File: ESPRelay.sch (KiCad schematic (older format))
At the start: 23 parts, among them J1 RELAY1, J2 RELAY2, J3 SENSOR_1, J4 SENSOR_2, K1 G5Q-1, K2 G5Q-1, Q1 2N3904, Q2 2N3904, U1 NodeMCU_1.0_(ESP-12E), U2 EL817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

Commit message: Fixed misconnected sensor inputs
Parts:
- U1: symbol ESP8266:NodeMCU_1.0_(ESP-12E) -> ESPRelay-rescue:NodeMCU_1.0_(ESP-12E)-ESP8266
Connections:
- net at U1.22 (D6(GPIO12)): now also J4.2 (Pin_2)
- net at U1.23 (D5(GPIO14)): now also J3.2 (Pin_2)
- net at U1.26 (D4(GPIO2)): no longer J4.2 (Pin_2)
- net at U1.27 (D3(GPIO0)): no longer J3.2 (Pin_2)
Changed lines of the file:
@@
 NoConn ~ 2700 3200
 NoConn ~ 2700 3500
-NoConn ~ 2700 3700
-NoConn ~ 2700 3800
 NoConn ~ 2700 3900
 NoConn ~ 2700 4000
@@
 NoConn ~ 1100 4200
 $Comp
-L ESP8266:NodeMCU_1.0_(ESP-12E) U1
+L ESPRelay-rescue:NodeMCU_1.0_(ESP-12E)-ESP8266 U1
 U 1 1 60060E77
 P 1900 3700
@@
 $EndComp
 Wire Wire Line
-	2700 3300 3500 3300
-Wire Wire Line
-	3500 3300 3500 3200
-Wire Wire Line
-	3500 3200 3850 3200
-Wire Wire Line
-	2700 3400 3500 3400
-Wire Wire Line
-	3500 3400 3500 3500
-Wire Wire Line
-	3500 3500 3850 3500
-Wire Wire Line
 	3750 2250 3750 3100
 Wire Wire Line
@@
 Wire Wire Line
 	3750 3100 3750 3300
+Wire Wire Line
+	2700 3700 3300 3700
+Wire Wire Line
+	3300 3700 3300 3200
+Wire Wire Line
+	3300 3200 3850 3200
+Wire Wire Line
+	2700 3800 3400 3800
+Wire Wire Line
+	3400 3800 3400 3500
+Wire Wire Line
+	3400 3500 3850 3500
+NoConn ~ 2700 3300
+NoConn ~ 2700 3400
 $EndSCHEMATC

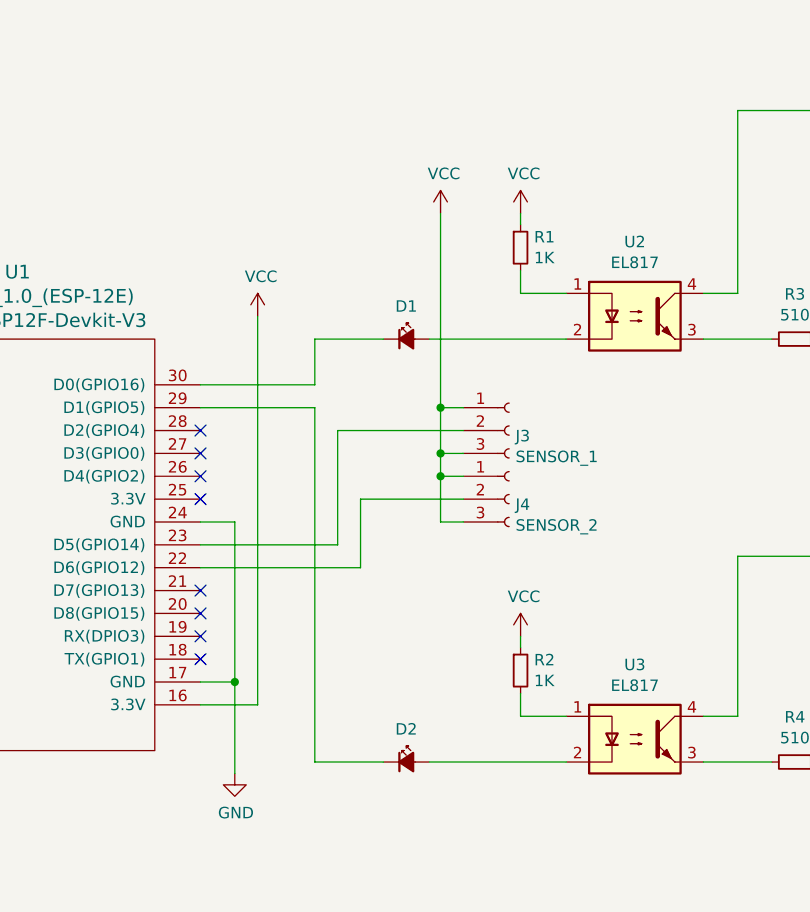
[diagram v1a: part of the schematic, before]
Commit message: Fix error with relay connections to NodeMCU. Include README.md and git ignore file.
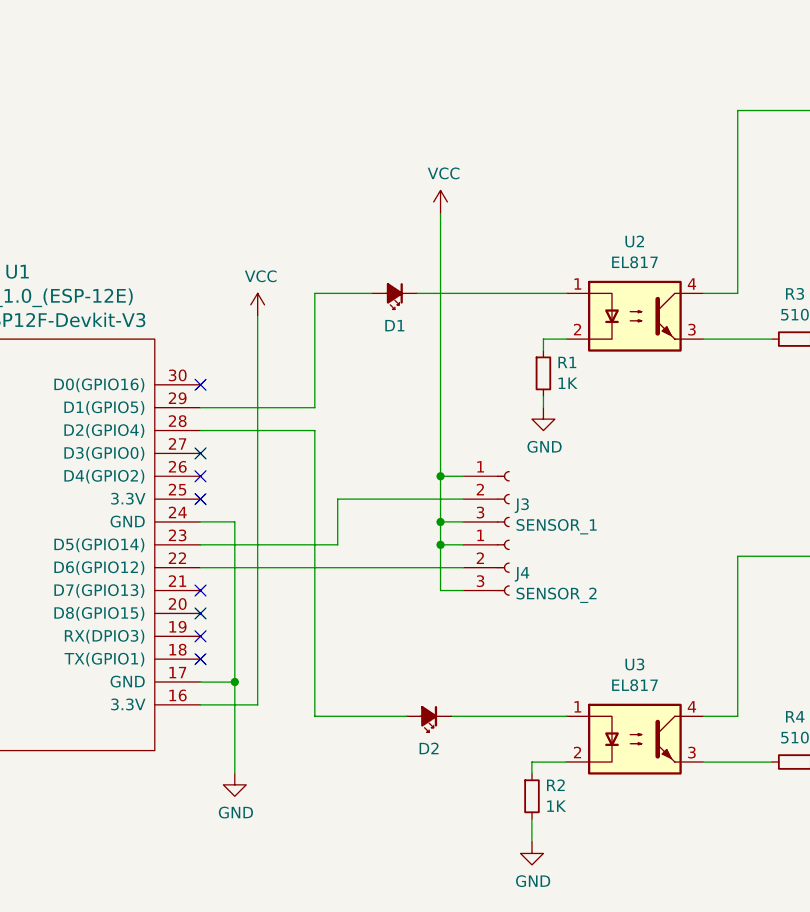
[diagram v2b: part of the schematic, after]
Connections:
- net GND: now also R1.2, R2.2
- net VCC: no longer R1.1, R2.1
- net at U2.1: now also D1.1 (K); no longer R1.2
- net at U2.2: now also R1.1; no longer D1.2 (A)
- net at U3.1: now also D2.1 (K); no longer R2.2
- net at U3.2: now also R2.1; no longer D2.2 (A)
- net at U1.30 (D0(GPIO16)): no longer D1.1 (K)
- net at U1.29 (D1(GPIO5)): now also D1.2 (A); no longer D2.1 (K)
- net at U1.28 (D2(GPIO4)): now also D2.2 (A)
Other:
- moved on the sheet: D1, D2, J3, J4, R1, R2
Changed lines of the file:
@@
 L Device:LED_Small_ALT D1
 U 1 1 60045D7A
-P 3600 2800
-F 0 "D1" H 3600 2943 50  0000 C CNN
-F 1 "LED_Small_ALT" H 3600 2944 50  0001 C CNN
-F 2 "LED_THT:LED_D5.0mm" V 3600 2800 50  0001 C CNN
-F 3 "~" V 3600 2800 50  0001 C CNN
-	1    3600 2800
-	1    0    0    -1
+P 3550 2600
+F 0 "D1" H 3550 2743 50  0000 C CNN
+F 1 "LED_Small_ALT" H 3550 2744 50  0001 C CNN
+F 2 "LED_THT:LED_D5.0mm" V 3550 2600 50  0001 C CNN
+F 3 "~" V 3550 2600 50  0001 C CNN
+	1    3550 2600
+	-1   0    0    1
 $EndComp
 $Comp
 L Device:LED_Small_ALT D2
 U 1 1 600472E3
-P 3600 4650
-F 0 "D2" H 3600 4793 50  0000 C CNN
-F 1 "LED_Small_ALT" H 3600 4794 50  0001 C CNN
-F 2 "LED_THT:LED_D5.0mm" V 3600 4650 50  0001 C CNN
-F 3 "~" V 3600 4650 50  0001 C CNN
-	1    3600 4650
-	1    0    0    -1
-$EndComp
-Wire Wire Line
-	2700 3000 3200 3000
-Wire Wire Line
-	3200 3000 3200 2800
-Wire Wire Line
-	3200 2800 3500 2800
-Wire Wire Line
-	2700 3100 3200 3100
-$Comp
-L power:VCC #PWR05
-U 1 1 6004C243
-P 4100 2250
-F 0 "#PWR05" H 4100 2100 50  0001 C CNN
-F 1 "VCC" H 4115 2423 50  0000 C CNN
-F 2 "" H 4100 2250 50  0001 C CNN
-F 3 "" H 4100 2250 50  0001 C CNN
-	1    4100 2250
-	1    0    0    -1
+P 3700 4450
+F 0 "D2" H 3700 4593 50  0000 C CNN
+F 1 "LED_Small_ALT" H 3700 4594 50  0001 C CNN
+F 2 "LED_THT:LED_D5.0mm" V 3700 4450 50  0001 C CNN
+F 3 "~" V 3700 4450 50  0001 C CNN
+	1    3700 4450
+	-1   0    0    1
 $EndComp
 $Comp
 L Device:R_Small R1
 U 1 1 6004D44F
-P 4100 2400
-F 0 "R1" H 4159 2446 50  0000 L CNN
-F 1 "1K" H 4159 2355 50  0000 L CNN
-F 2 "Resistor_THT:R_Axial_DIN0204_L3.6mm_D1.6mm_P5.08mm_Horizontal" H 4100 2400 50  0001 C CNN
-F 3 "~" H 4100 2400 50  0001 C CNN
-	1    4100 2400
+P 4200 2950
+F 0 "R1" H 4259 2996 50  0000 L CNN
+F 1 "1K" H 4259 2905 50  0000 L CNN
+F 2 "Resistor_THT:R_Axial_DIN0204_L3.6mm_D1.6mm_P5.08mm_Horizontal" H 4200 2950 50  0001 C CNN
+F 3 "~" H 4200 2950 50  0001 C CNN
+	1    4200 2950
 	1    0    0    -1
 $EndComp
@@
 L Device:R_Small R2
 U 1 1 6004E54C
-P 4100 4250
-F 0 "R2" H 4159 4296 50  0000 L CNN
-F 1 "1K" H 4159 4205 50  0000 L CNN
-F 2 "Resistor_THT:R_Axial_DIN0204_L3.6mm_D1.6mm_P5.08mm_Horizontal" H 4100 4250 50  0001 C CNN
-F 3 "~" H 4100 4250 50  0001 C CNN
-	1    4100 4250
-	1    0    0    -1
-$EndComp
-Wire Wire Line
-	3200 4650 3500 4650
-Wire Wire Line
-	4100 2500 4100 2600
-Wire Wire Line
-	4100 2600 4300 2600
-Wire Wire Line
-	4100 4350 4100 4450
-Wire Wire Line
-	4100 4450 4300 4450
-$Comp
-L power:VCC #PWR06
-U 1 1 60052A70
-P 4100 4100
-F 0 "#PWR06" H 4100 3950 50  0001 C CNN
-F 1 "VCC" H 4115 4273 50  0000 C CNN
-F 2 "" H 4100 4100 50  0001 C CNN
-F 3 "" H 4100 4100 50  0001 C CNN
-	1    4100 4100
-	1    0    0    -1
-$EndComp
-Wire Wire Line
-	4100 2250 4100 2300
-Wire Wire Line
-	4100 4100 4100 4150
-Wire Wire Line
-	3700 4650 4300 4650
-Wire Wire Line
-	3700 2800 4300 2800
+P 4150 4800
+F 0 "R2" H 4209 4846 50  0000 L CNN
+F 1 "1K" H 4209 4755 50  0000 L CNN
+F 2 "Resistor_THT:R_Axial_DIN0204_L3.6mm_D1.6mm_P5.08mm_Horizontal" H 4150 4800 50  0001 C CNN
+F 3 "~" H 4150 4800 50  0001 C CNN
+	1    4150 4800
+	1    0    0    -1
+$EndComp
 $Comp
 L Device:R_Small R3
@@
 	0    1    1    0
 $EndComp
-Wire Wire Line
-	3200 3100 3200 4650
 $Comp
 L Diode:1N4003 D4
@@
 NoConn ~ 1100 3700
 NoConn ~ 1100 3800
-NoConn ~ 2700 3200
 NoConn ~ 2700 3500
 NoConn ~ 2700 3900
@@
 L Connector:Conn_01x03_Female J3
 U 1 1 600FD4AA
-P 4050 3200
-F 0 "J3" H 4078 3176 50  0000 L CNN
-F 1 "SENSOR_1" H 4078 3085 50  0000 L CNN
-F 2 "TerminalBlock_TE-Connectivity:TerminalBlock_TE_282834-3_1x03_P2.54mm_Horizontal" H 4050 3200 50  0001 C CNN
-F 3 "~" H 4050 3200 50  0001 C CNN
-	1    4050 3200
-	1    0    0    -1
-$EndComp
-$Comp
-L Connector:Conn_01x03_Female J4
-U 1 1 60100DDF
 P 4050 3500
-F 0 "J4" H 4078 3476 50  0000 L CNN
-F 1 "SENSOR_2" H 4078 3385 50  0000 L CNN
+F 0 "J3" H 4078 3476 50  0000 L CNN
+F 1 "SENSOR_1" H 4078 3385 50  0000 L CNN
 F 2 "TerminalBlock_TE-Connectivity:TerminalBlock_TE_282834-3_1x03_P2.54mm_Horizontal" H 4050 3500 50  0001 C CNN
 F 3 "~" H 4050 3500 50  0001 C CNN
 	1    4050 3500
+	1    0    0    -1
+$EndComp
+$Comp
+L Connector:Conn_01x03_Female J4
+U 1 1 60100DDF
+P 4050 3800
+F 0 "J4" H 4078 3776 50  0000 L CNN
+F 1 "SENSOR_2" H 4078 3685 50  0000 L CNN
+F 2 "TerminalBlock_TE-Connectivity:TerminalBlock_TE_282834-3_1x03_P2.54mm_Horizontal" H 4050 3800 50  0001 C CNN
+F 3 "~" H 4050 3800 50  0001 C CNN
+	1    4050 3800
 	1    0    0    -1
 $EndComp
@@
 $EndComp
 Wire Wire Line
-	3750 2250 3750 3100
-Wire Wire Line
-	3750 3600 3850 3600
+	3750 3900 3850 3900
+Wire Wire Line
+	3850 3700 3750 3700
+Connection ~ 3750 3700
+Wire Wire Line
+	3750 3700 3750 3900
+Wire Wire Line
+	3850 3600 3750 3600
+Connection ~ 3750 3600
+Wire Wire Line
+	3750 3600 3750 3700
 Wire Wire Line
 	3850 3400 3750 3400
@@
 	3750 3400 3750 3600
 Wire Wire Line
-	3850 3300 3750 3300
-Connection ~ 3750 3300
-Wire Wire Line
-	3750 3300 3750 3400
-Wire Wire Line
-	3850 3100 3750 3100
-Connection ~ 3750 3100
-Wire Wire Line
-	3750 3100 3750 3300
-Wire Wire Line
 	2700 3700 3300 3700
 Wire Wire Line
-	3300 3700 3300 3200
-Wire Wire Line
-	3300 3200 3850 3200
-Wire Wire Line
-	2700 3800 3400 3800
-Wire Wire Line
-	3400 3800 3400 3500
-Wire Wire Line
-	3400 3500 3850 3500
+	3300 3700 3300 3500
 NoConn ~ 2700 3300
 NoConn ~ 2700 3400
+Wire Wire Line
+	2700 3200 3200 3200
+Wire Wire Line
+	2700 3100 3200 3100
+NoConn ~ 2700 3000
+Wire Wire Line
+	3600 4450 3200 4450
+Wire Wire Line
+	3200 4450 3200 3200
+Wire Wire Line
+	3800 4450 4300 4450
+$Comp
+L power:GND #PWR?
+U 1 1 60D67460
+P 4150 5000
+F 0 "#PWR?" H 4150 4750 50  0001 C CNN
+F 1 "GND" H 4155 4827 50  0000 C CNN
+F 2 "" H 4150 5000 50  0001 C CNN
+F 3 "" H 4150 5000 50  0001 C CNN
+	1    4150 5000
+	1    0    0    -1
+$EndComp
+Wire Wire Line
+	4150 5000 4150 4900
+Wire Wire Line
+	4300 4650 4150 4650
+Wire Wire Line
+	4150 4650 4150 4700
+Wire Wire Line
+	3200 3100 3200 2600
+Wire Wire Line
+	3200 2600 3450 2600
+Wire Wire Line
+	3650 2600 4300 2600
+$Comp
+L power:GND #PWR?
+U 1 1 60D751B4
+P 4200 3100
+F 0 "#PWR?" H 4200 2850 50  0001 C CNN
+F 1 "GND" H 4205 2927 50  0000 C CNN
+F 2 "" H 4200 3100 50  0001 C CNN
+F 3 "" H 4200 3100 50  0001 C CNN
+	1    4200 3100
+	1    0    0    -1
+$EndComp
+Wire Wire Line
+	2700 3800 3850 3800
+Wire Wire Line
+	3300 3500 3850 3500
+Wire Wire Line
+	3750 2250 3750 3400
+Wire Wire Line
+	4300 2800 4200 2800
+Wire Wire Line
+	4200 2800 4200 2850
+Wire Wire Line
+	4200 3050 4200 3100
 $EndSCHEMATC
